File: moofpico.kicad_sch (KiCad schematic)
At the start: 21 parts, among them J1 Conn_01x05, J100 Bus_Apple_II_Card_Side, J2 Micro_SD_Card_Det2, Q1 BS170, SW2 SW_DIP_x02, U1 Pico, U2 74F11, U3 74LVC245, U4 74LVC245, U5 74LVC245

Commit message: remove the interior two layers; should have never been there to begin with
notey notey note
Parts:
- J1: footprint Connector_PinSocket_2.00mm:PinSocket_1x05_P2.00mm_Vertical -> Connector_PinHeader_2.00mm:PinHeader_1x05_P2.00mm_Vertical
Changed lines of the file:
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@@
 			)
 		)
-		(property "Footprint" "Connector_PinSocket_2.00mm:PinSocket_1x05_P2.00mm_Vertical"
+		(property "Footprint" "Connector_PinHeader_2.00mm:PinHeader_1x05_P2.00mm_Vertical"
 			(at 102.87 24.13 0)
 			(effects

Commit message: checkpoint: moved the SD card around
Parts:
- removed J1: Conn_01x05, Connector_PinHeader_2.00mm:PinHeader_1x05_P2.00mm_Vertical, symbol Connector_Generic:Conn_01x05
- added J1: Conn_01x04, Connector_PinHeader_1.27mm:PinHeader_1x04_P1.27mm_Vertical, symbol Connector_Generic:Conn_01x04
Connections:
- net GND: now also J1.1 (Pin_1)
- net at U1.2 (GPIO1): now also J1.3 (Pin_3)
- net at U1.1 (GPIO0): now also J1.4 (Pin_4)
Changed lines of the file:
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@@
 	)
 	(no_connect
+		(at 102.87 29.21)
+	)
+	(no_connect
 		(at 146.05 82.55)
 	)
@@
 	)
 	(no_connect
-		(at 100.33 29.21)
-	)
-	(no_connect
 		(at 196.85 80.01)
 	)
@@
 	(wire
 		(pts
+			(xy 105.41 29.21) (xy 105.41 31.75)
+		)
+		(stroke
+			(width 0)
+			(type default)
+		)
+	)
+	(wire
+		(pts
 			(xy 166.37 31.75) (xy 200.66 31.75)
 		)
@@
 	(wire
 		(pts
-			(xy 105.41 31.75) (xy 130.81 31.75)
-		)
-		(stroke
-			(width 0)
-			(type default)
-		)
-	)
-	(wire
-		(pts
 			(xy 73.66 87.63) (xy 73.66 90.17)
 		)
@@
 	(wire
 		(pts
-			(xy 105.41 29.21) (xy 105.41 31.75)
+			(xy 105.41 31.75) (xy 130.81 31.75)
 		)
 		(stroke
@@
 	)
 	(symbol
-		(lib_id "Connector_Generic:Conn_01x05")
-		(at 102.87 24.13 90)
-		(unit 1)
-		(exclude_from_sim no)
-		(in_bom yes)
-		(on_board yes)
-		(dnp no)
-		(fields_autoplaced yes)
-		(property "Reference" "J1"
-			(at 102.87 17.78 90)
-			(effects
-				(font
-					(size 1.27 1.27)
-				)
-			)
-		)
-		(property "Value" "Conn_01x05"
-			(at 102.87 20.32 90)
-			(effects
-				(font
-					(size 1.27 1.27)
-				)
-			)
-		)
-		(property "Footprint" "Connector_PinHeader_2.00mm:PinHeader_1x05_P2.00mm_Vertical"
-			(at 102.87 24.13 0)
-			(effects
-				(font
-					(size 1.27 1.27)
-				)
-				(hide yes)
-			)
-		)
-		(property "Datasheet" "~"
-			(at 102.87 24.13 0)
-			(effects
-				(font
-					(size 1.27 1.27)
-				)
-				(hide yes)
-			)
-		)
-		(property "Description" "Generic connector, single row, 01x05, script generated (kicad-library-utils/schlib/autogen/connector/)"
-			(at 102.87 24.13 0)
-			(effects
-				(font
-					(size 1.27 1.27)
-				)
-				(hide yes)
-			)
-		)
-		(pin "5"
-		)
-		(pin "3"
-		)
-		(pin "1"
-		)
-		(pin "4"
-		)
-		(pin "2"
-		)
-		(instances
-			(project "moofpico"
-				(path "/adf04048-7c47-4d7c-943c-c55ccf696419"
-					(reference "J1")
-					(unit 1)
-				)
-			)
-		)
-	)
-	(symbol
 		(lib_id "power:GND")
 		(at 226.06 123.19 0)
@@
 	)
 	(symbol
+		(lib_id "Connector_Generic:Conn_01x04")
+		(at 102.87 24.13 90)
+		(unit 1)
+		(exclude_from_sim no)
+		(in_bom yes)
+		(on_board yes)
+		(dnp no)
+		(fields_autoplaced yes)
+		(property "Reference" "J1"
+			(at 104.14 17.78 90)
+			(effects
+				(font
+					(size 1.27 1.27)
+				)
+			)
+		)
+		(property "Value" "Conn_01x04"
+			(at 104.14 20.32 90)
+			(effects
+				(font
+					(size 1.27 1.27)
+				)
+			)
+		)
+		(property "Footprint" "Connector_PinHeader_1.27mm:PinHeader_1x04_P1.27mm_Vertical"
+			(at 102.87 24.13 0)
+			(effects
+				(font
+					(size 1.27 1.27)
+				)
+				(hide yes)
+			)
+		)
+		(property "Datasheet" "~"
+			(at 102.87 24.13 0)
+			(effects
+				(font
+					(size 1.27 1.27)
+				)
+				(hide yes)
+			)
+		)
+		(property "Description" "Generic connector, single row, 01x04, script generated (kicad-library-utils/schlib/autogen/connector/)"
+			(at 102.87 24.13 0)
+			(effects
+				(font
+					(size 1.27 1.27)
+				)
+				(hide yes)
+			)
+		)
+		(pin "2"
+		)
+		(pin "3"
+		)
+		(pin "1"
+		)
+		(pin "4"
+		)
+		(instances
+			(project "moofpico"
+				(path "/adf04048-7c47-4d7c-943c-c55ccf696419"
+					(reference "J1")
+					(unit 1)
+				)
+			)
+		)
+	)
+	(symbol
 		(lib_id "power:+3V3")
 		(at 76.2 74.93 180)
@@
 	(symbol
 		(lib_id "power:GND")
-		(at 97.79 29.21 0)
+		(at 100.33 29.21 0)
 		(unit 1)
 		(exclude_from_sim no)
@@
 		(fields_autoplaced yes)
 		(property "Reference" "#PWR02"
-			(at 97.79 35.56 0)
+			(at 100.33 35.56 0)
 			(effects
 				(font
@@
 		)
 		(property "Value" "GND"
-			(at 97.79 34.29 0)
+			(at 100.33 34.29 0)
 			(effects
 				(font
@@
 		)
 		(property "Footprint" ""
-			(at 97.79 29.21 0)
+			(at 100.33 29.21 0)
 			(effects
 				(font
@@
 		)
 		(property "Datasheet" ""
-			(at 97.79 29.21 0)
+			(at 100.33 29.21 0)
 			(effects
 				(font
@@
 		)
 		(property "Description" "Power symbol creates a global label with name \"GND\" , ground"
-			(at 97.79 29.21 0)
+			(at 100.33 29.21 0)
 			(effects
 				(font
@@
 					(unit 1)
 				)
-			)
-		)
-	)
-	(symbol
-		(lib_id "power:+3V3")
-		(at 102.87 29.21 180)
-		(unit 1)
-		(exclude_from_sim no)
-		(in_bom yes)
-		(on_board yes)
-		(dnp no)
-		(fields_autoplaced yes)
-		(property "Reference" "#PWR06"
-			(at 102.87 25.4 0)
-			(effects
-				(font
-					(size 1.27 1.27)
-				)
-				(hide yes)
-			)
-		)
-		(property "Value" "+3V3"
-			(at 102.87 34.29 0)
-			(effects
-				(font
-					(size 1.27 1.27)
-				)
-			)
-		)
-		(property "Footprint" ""
-			(at 102.87 29.21 0)
-			(effects
-				(font
-					(size 1.27 1.27)
-				)
-				(hide yes)
-			)
-		)
-		(property "Datasheet" ""
-			(at 102.87 29.21 0)
-			(effects
-				(font
-					(size 1.27 1.27)
-				)
-				(hide yes)
-			)
-		)
-		(property "Description" "Power symbol creates a global label with name \"+3V3\""
-			(at 102.87 29.21 0)
-			(effects
-				(font
-					(size 1.27 1.27)
-				)
-				(hide yes)
-			)
-		)
-		(pin "1"
-		)
-		(instances
-			(project "moofpico"
-				(path "/adf04048-7c47-4d7c-943c-c55ccf696419"
-					(reference "#PWR06")
-					(unit 1)
-				)

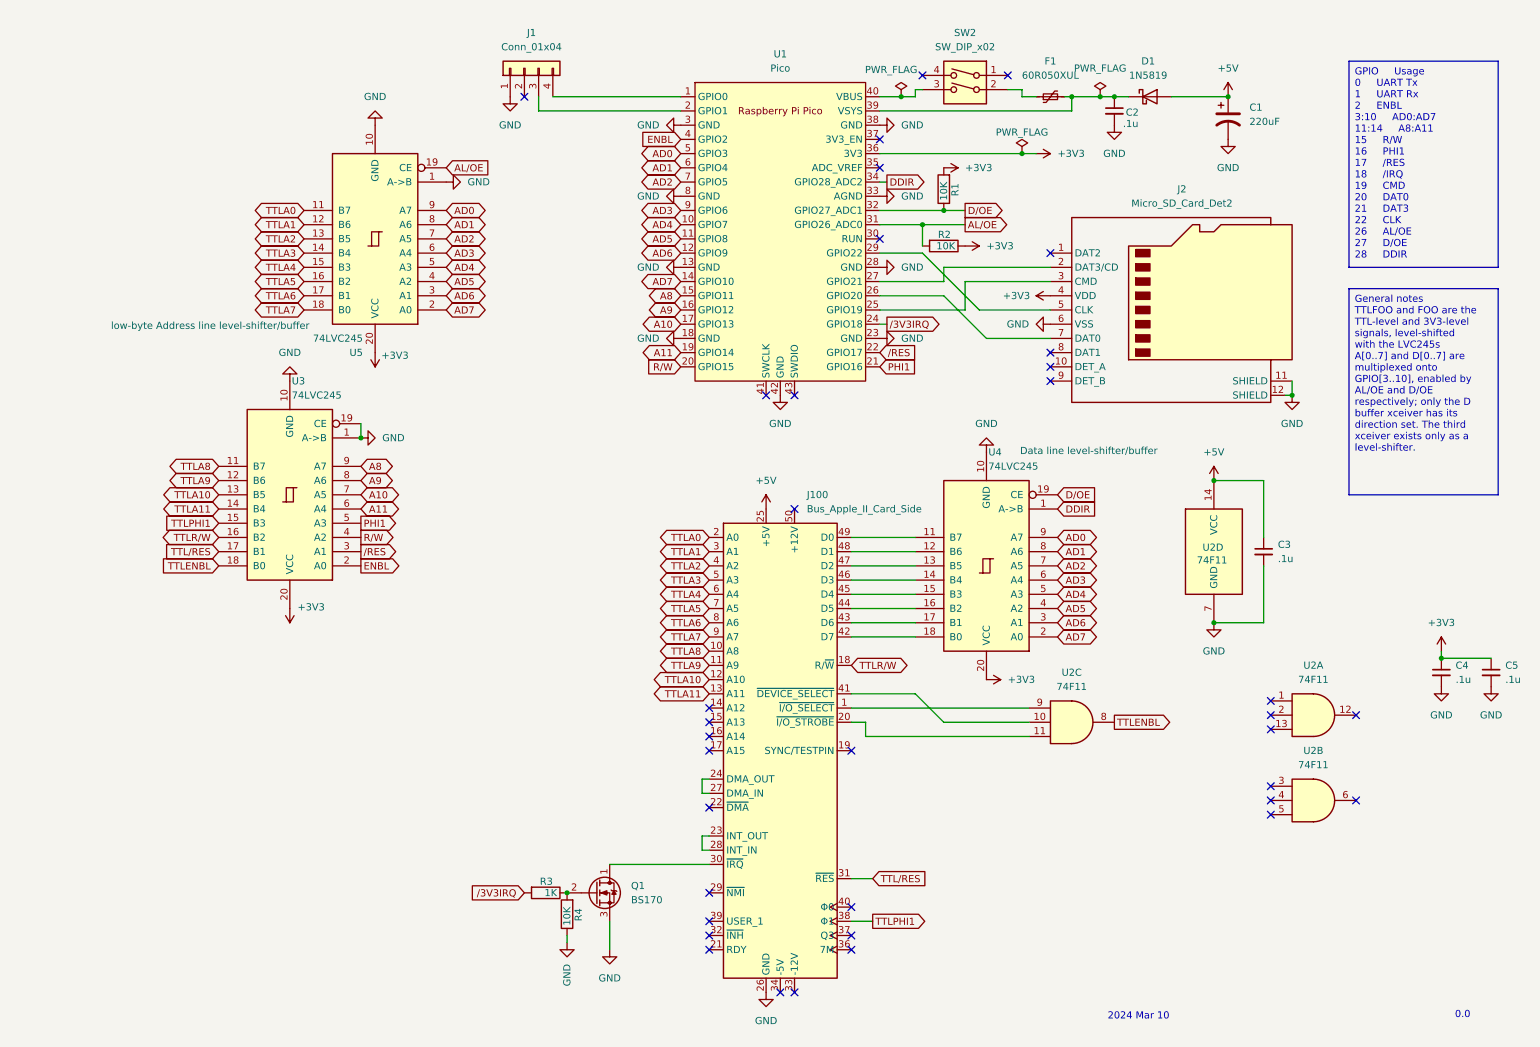
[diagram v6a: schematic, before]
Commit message: use ki-lime-pi-pico footprint, since it has a bunch of extra stuff (keepouts and holes) - which required rerouting a whole bunch of stuff
labels, whee
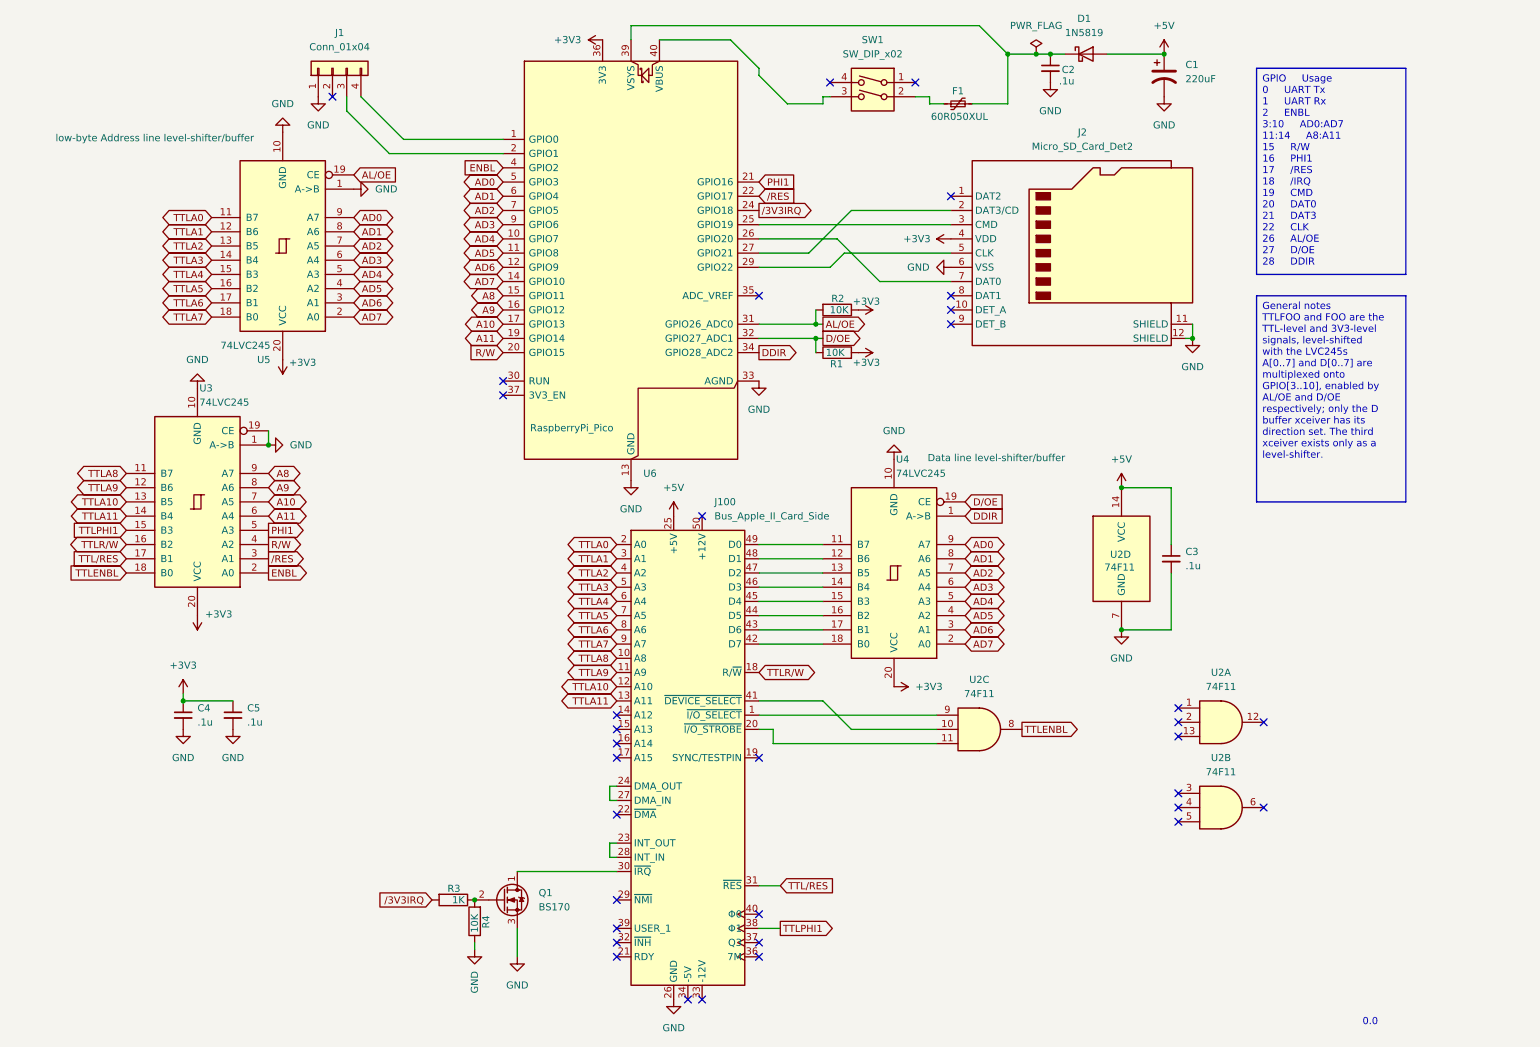
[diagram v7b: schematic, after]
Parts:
- removed U1: Pico, MCU_RaspberryPi_and_Boards:RPi_Pico_SMD_TH, symbol MCU_RaspberryPi_and_Boards:Pico
- added U6: RaspberryPi_Pico, Module_RaspberryPi_Pico:RaspberryPi_Pico_Common, symbol MCU_Module_RaspberryPi_Pico:RaspberryPi_Pico
- renumbered SW2 to SW1
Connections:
- net +3V3: now also U6.36 (3V3)
- net A10: now also U6.17 (GPIO13)
- net A11: now also U6.19 (GPIO14)
- net A8: now also U6.15 (GPIO11)
- net A9: now also U6.16 (GPIO12)
- net AD0: now also U6.5 (GPIO3)
- net AD1: now also U6.6 (GPIO4)
- net AD2: now also U6.7 (GPIO5)
- net AD3: now also U6.9 (GPIO6)
- net AD4: now also U6.10 (GPIO7)
- net AD5: now also U6.11 (GPIO8)
- net AD6: now also U6.12 (GPIO9)
- net AD7: now also U6.14 (GPIO10)
- net AL/OE: now also U6.31 (GPIO26_ADC0)
- net DDIR: now also U6.34 (GPIO28_ADC2)
- net D/OE: now also U6.32 (GPIO27_ADC1)
- net ENBL: now also U6.4 (GPIO2)
- net GND: now also U6.13 (GND), U6.18 (GND), U6.23 (GND), U6.28 (GND), U6.3 (GND), U6.33 (AGND), U6.38 (GND), U6.8 (GND)
- net PHI1: now also U6.21 (GPIO16)
- net R/W: now also U6.20 (GPIO15)
- net /3V3‏IRQ: now also U6.24 (GPIO18)
- net /RES: now also U6.22 (GPIO17)
- net at J1.3 (Pin_3): now also U6.2 (GPIO1)
- net at J1.4 (Pin_4): now also U6.1 (GPIO0)
- net at C2.1, D1.1 (K), F1.2: now also U6.39 (VSYS)
- net at J2.3 (CMD): now also U6.25 (GPIO19)
- net at J2.7 (DAT0): now also U6.26 (GPIO20)
- net at J2.2 (DAT3/CD): now also U6.27 (GPIO21)
- net at J2.5 (CLK): now also U6.29 (GPIO22)
- net at SW1.3: now also U6.40 (VBUS)
- no-connect marks 36 -> 34
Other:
- note removed: "2024 Mar 10"
- title: (none) -> moofpico
- moved on the sheet: C1, C2, C3, C4, C5, D1, F1, J1, J100, J2, Q1, R1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

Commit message: more faffing about with moving components
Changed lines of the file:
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@@
 		)
 		(property "Value" "1K"
-			(at 92.202 172.72 90)
+			(at 91.44 172.72 90)
 			(effects
 				(font
